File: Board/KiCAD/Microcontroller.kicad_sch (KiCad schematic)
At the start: 26 parts, among them J2 Conn_ARM_SWD_TagConnect_TC2030, J3 Boot, SW2 SW_Push, U10 RT9193-33GB, U2 MIC4680, U9 STM32F103C8T6, Y4 CM8V-T1A-32.768KHZ-12.5PF-20P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, Y5 8MHz

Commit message: Add files via upload
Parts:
- removed C11, C29: 1uF, Capacitor_SMD:C_0201_0603Metric, symbol Device:C_Small
- removed C28: 22nF, Capacitor_SMD:C_0201_0603Metric, symbol Device:C_Small
- removed C45: 15uF, Capacitor_SMD:C_0201_0603Metric, symbol Device:C_Small
- removed C46: ~, Capacitor_SMD:C_0201_0603Metric, symbol Device:C_Small
- removed D1: B260, Diode_SMD:D_SMB, symbol Diode:B260
- removed L1: 10uH, symbol Device:L_Small
- removed R72: 3k, Resistor_SMD:R_0201_0603Metric, symbol Device:R_Small
- removed R73: 1k, Resistor_SMD:R_0201_0603Metric, symbol Device:R_Small
- removed U10: RT9193-33GB, Package_TO_SOT_SMD:SOT-23-5, symbol RT9193-33GB:RT9193-33GB
- removed U2: MIC4680, Package_SO:SOIC-8-1EP_3.9x4.9mm_P1.27mm_EP2.41x3.3mm_ThermalVias, symbol MIC4680:MIC4680
- added C51, C52, C53: 15uF, Capacitor_SMD:C_0201_0603Metric, symbol Device:C_Small
- added L3: 10uH, symbol Device:L_Small
- added U5: LMR50410, Package_TO_SOT_SMD:SOT-23-6, symbol Regulator_Switching:LMR50410
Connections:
- net 3.3V: now also C53.1, L3.2, U5.3 (FB)
- net GND: now also C51.2, C53.2, U5.2 (GND)
- net Vin: now also C51.1, U5.4 (EN), U5.5 (VIN)
- net Thermistor C1: now reaches U9.12 (PA2)
- net Thermistor C2: now reaches U9.13 (PA3)
- net Thermistor C3: now reaches U9.14 (PA4)
- net Thermistor C4: now reaches U9.15 (PA5)
- net SWDIO: now reaches U9.34 (PA13)
- net SWDIO: now also J2.2 (SWDIO), J2.6 (SWO)
- net SWCLK: now reaches U9.37 (PA14)
- net SWCLK: now also J2.4 (SWCLK)
- new net: C52.1, U5.1 (CB)
- new net: C52.2, L3.1, U5.6 (SW)
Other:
- note removed: "Why in the world are you doing an SPS to an LDO? Don't do this, it's expensive, takes realestate, and you absolutely do not need the analog precision this gives. In fact, you're killing the quiet analog supply by connecting it to a microcontroller. So: replace this with a small, simple, SPS that only outputs 3.3V at less than 500 mA."
- moved on the sheet: C30, C31, C32, C33, C34, J2, J3, R58, R59, R60, R75, SW2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

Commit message: Add files via upload
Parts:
- removed J3: Boot, symbol Connector_Generic:Conn_02x03_Top_Bottom
- removed R59: 100k, Resistor_SMD:R_0201_0603Metric, symbol Device:R_Small
- added J4: Conn_01x03, Connector_PinHeader_1.00mm:PinHeader_1x03_P1.00mm_Vertical, symbol Connector_Generic:Conn_01x03
- C34: value 100n -> 100nF
- C51: value 15uF -> 2.2uF
- C52, C53: value 15uF -> 10uF
- L3: value 10uH -> 3.3uH; footprint (none) -> Inductor_SMD:L_10.4x10.4_H4.8
- SW2: footprint (none) -> Button_Switch_SMD:SW_Push_1P1T_NO_CK_KMR2
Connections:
- net 3.3V: now also J4.1 (Pin_1)
- net GND: now also J4.3 (Pin_3)
- net at R58.1: now also J4.2 (Pin_2)
- net Boot1: no longer names the net of U9.20 (PB2)
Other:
- note removed: "You don't need BOOT1"

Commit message: Add files via upload
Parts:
- L3: footprint Inductor_SMD:L_10.4x10.4_H4.8 -> Inductor_SMD:L_1008_2520Metric_Pad1.43x2.20mm_HandSolder
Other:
- note removed: "CONNECT ME"
- note removed: "Can this just be a push button? Like Reset?"
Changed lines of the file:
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@@
 		(comment 3 "Capstone - Team #6")
-	)
-	(text "Can this just be a push button?\nLike Reset?"
-		(exclude_from_sim no)
-		(at 176.53 59.69 0)
-		(effects
-			(font
-				(size 1.27 1.27)
-			)
-		)
 	)
 	(text "LEDS! GIVE ME LEDS! So many status LEDs!"
@@
 		(exclude_from_sim no)
 		(at 171.45 111.76 0)
-		(effects
-			(font
-				(size 1.27 1.27)
-			)
-		)
-	)
-	(text "CONNECT ME"
-		(exclude_from_sim no)
-		(at 151.13 50.8 0)
 		(effects
 			(font
@@
 			)
 		)
-		(property "Footprint" "Inductor_SMD:L_10.4x10.4_H4.8"
+		(property "Footprint" "Inductor_SMD:L_1008_2520Metric_Pad1.43x2.20mm_HandSolder"
 			(at 76.2 45.72 0)
 			(effects

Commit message: Add files via upload
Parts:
- C30, C31, C32, C33, C34, C51: footprint Capacitor_SMD:C_0201_0603Metric -> Capacitor_SMD:C_0603_1608Metric
- C52, C53: footprint Capacitor_SMD:C_0201_0603Metric -> Capacitor_SMD:C_1206_3216Metric; MFR (none) -> SAMSUNG; MPN (none) -> CL31A106KBHNNNE
- J4: footprint Connector_PinHeader_1.00mm:PinHeader_1x03_P1.00mm_Vertical -> Connector_PinHeader_2.54mm:PinHeader_1x03_P2.54mm_Vertical
- R58, R60, R75: footprint Resistor_SMD:R_0201_0603Metric -> Resistor_SMD:R_0603_1608Metric
- U9: MF STMicroelectronics -> (none); MFR (none) -> STMicroelectronics; MP STM32F103C8T6 -> (none); MPN (none) -> STM32F103C8T6
- Y4: MF Micro Crystal AG -> (none); MFR (none) -> Micro Crystal AG; MP CM8V-T1A-32.768KHZ-12.5PF-20PPM-TA-QA -> (none); MPN (none) -> CM8V-T1A-32.768KHZ-12.5PF-20PPM-TA-QA
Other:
- note removed: "LEDS! GIVE ME LEDS! So many status LEDs!"
- note removed: "Power LEDs! Give me all the power LEDs!"
- note removed: "SWD connector, "Tag Connect"."
- moved on the sheet: J2

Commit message: Updated Schematic & PCB Layout
Updated the look of the PCB layout to make the power flow Vin more intuitive.

@KeytarGoblin
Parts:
- C51: footprint Capacitor_SMD:C_0603_1608Metric -> Capacitor_SMD:C_1206_3216Metric
- Y5: footprint Crystal:Crystal_HC49-4H_Vertical -> Crystal:Crystal_SMD_5032-2Pin_5.0x3.2mm
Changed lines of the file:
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@@
 			)
 		)
-		(property "Footprint" "Capacitor_SMD:C_0603_1608Metric"
+		(property "Footprint" "Capacitor_SMD:C_1206_3216Metric"
 			(at 40.64 44.45 0)
 			(effects
@@
 			)
 		)
-		(property "Footprint" "Crystal:Crystal_HC49-4H_Vertical"
+		(property "Footprint" "Crystal:Crystal_SMD_5032-2Pin_5.0x3.2mm"
 			(at 74.93 170.18 0)
 			(effects

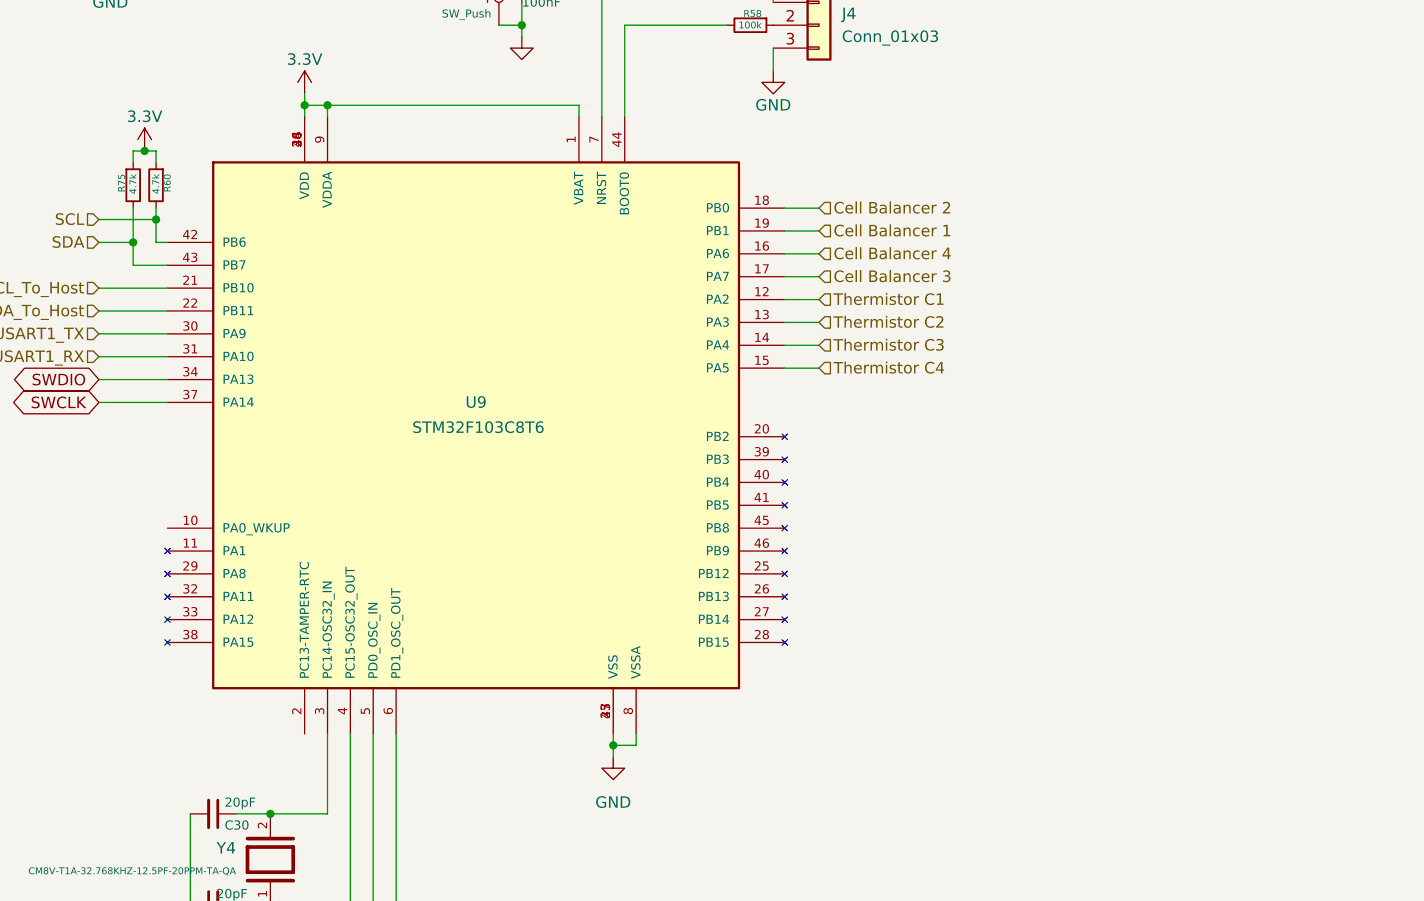
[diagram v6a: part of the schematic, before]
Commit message: Schematic: - Fixed FDI plug - Added thermistor connectors - Added a bunch of NCs using KiCAD NC tool - Added filter cap back into battery current shunt - Added bypass cap to LTC - Removed Cell 4 INA260 because the LTC does current, voltage of that top cell! Board Layout: - Chewed out team for not reading the BQ's datasheet, specifically Section 11 - Relayed out power stream using Section 11 as a refernce - Changed some footprints, mostly reducing size to 0603 - Positioned things optimally given what I thought made sense (dangerous, I know) - Fixed ground planes Other: - Removed PRL and CACHE files from the repo.
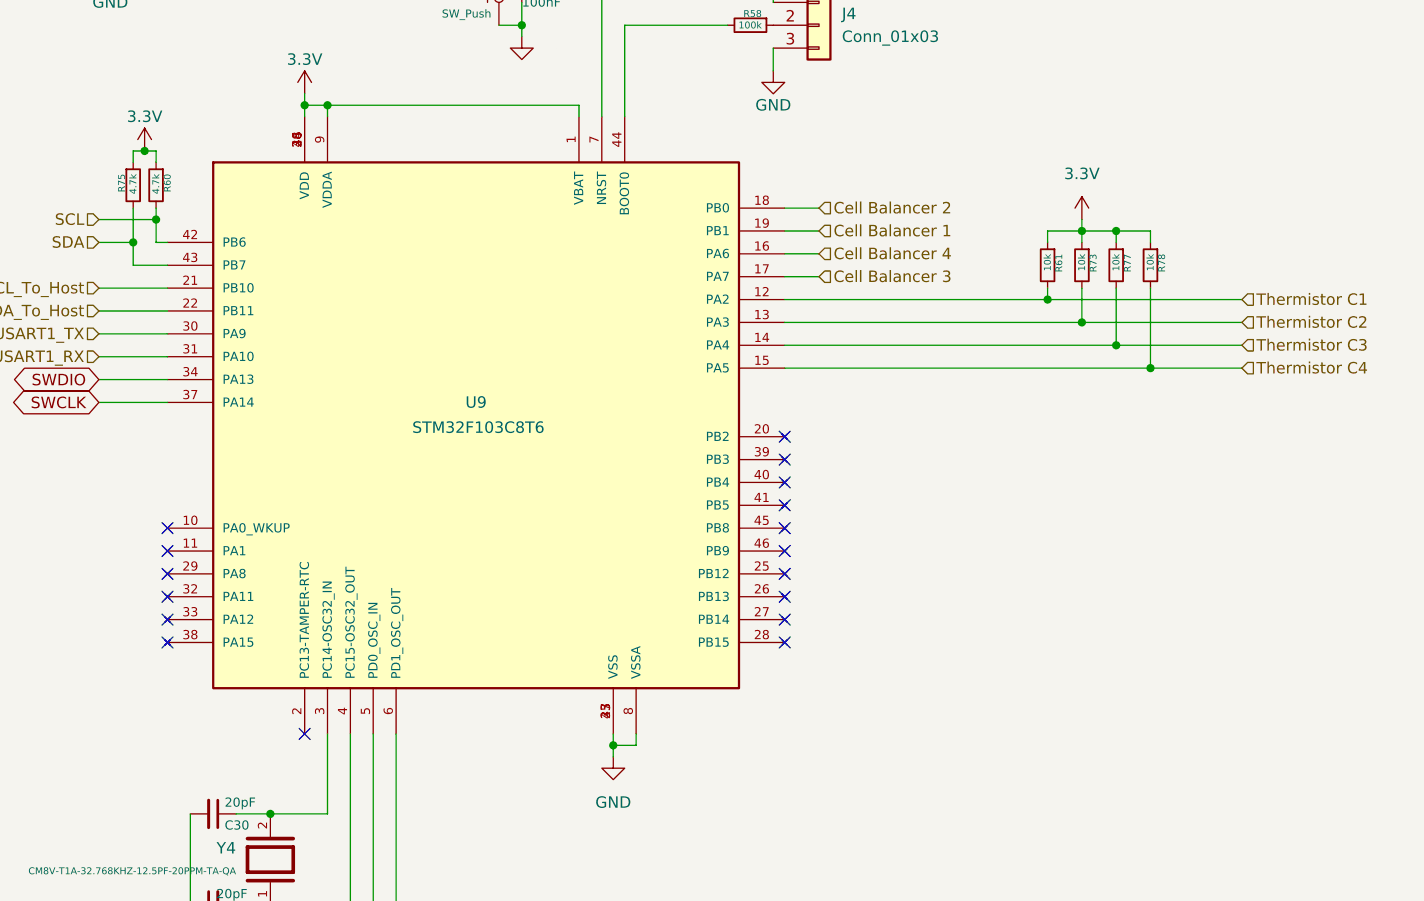
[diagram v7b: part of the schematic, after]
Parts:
- added R61, R73, R77, R78: 10k, Resistor_SMD:R_0603_1608Metric, symbol Device:R_Small
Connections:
- net 3.3V: now also R61.1, R73.1, R77.1, R78.1
- net Thermistor C1: now also R61.2
- net Thermistor C2: now also R73.2
- net Thermistor C3: now also R77.2
- net Thermistor C4: now also R78.2
- no-connect marks 0 -> 17

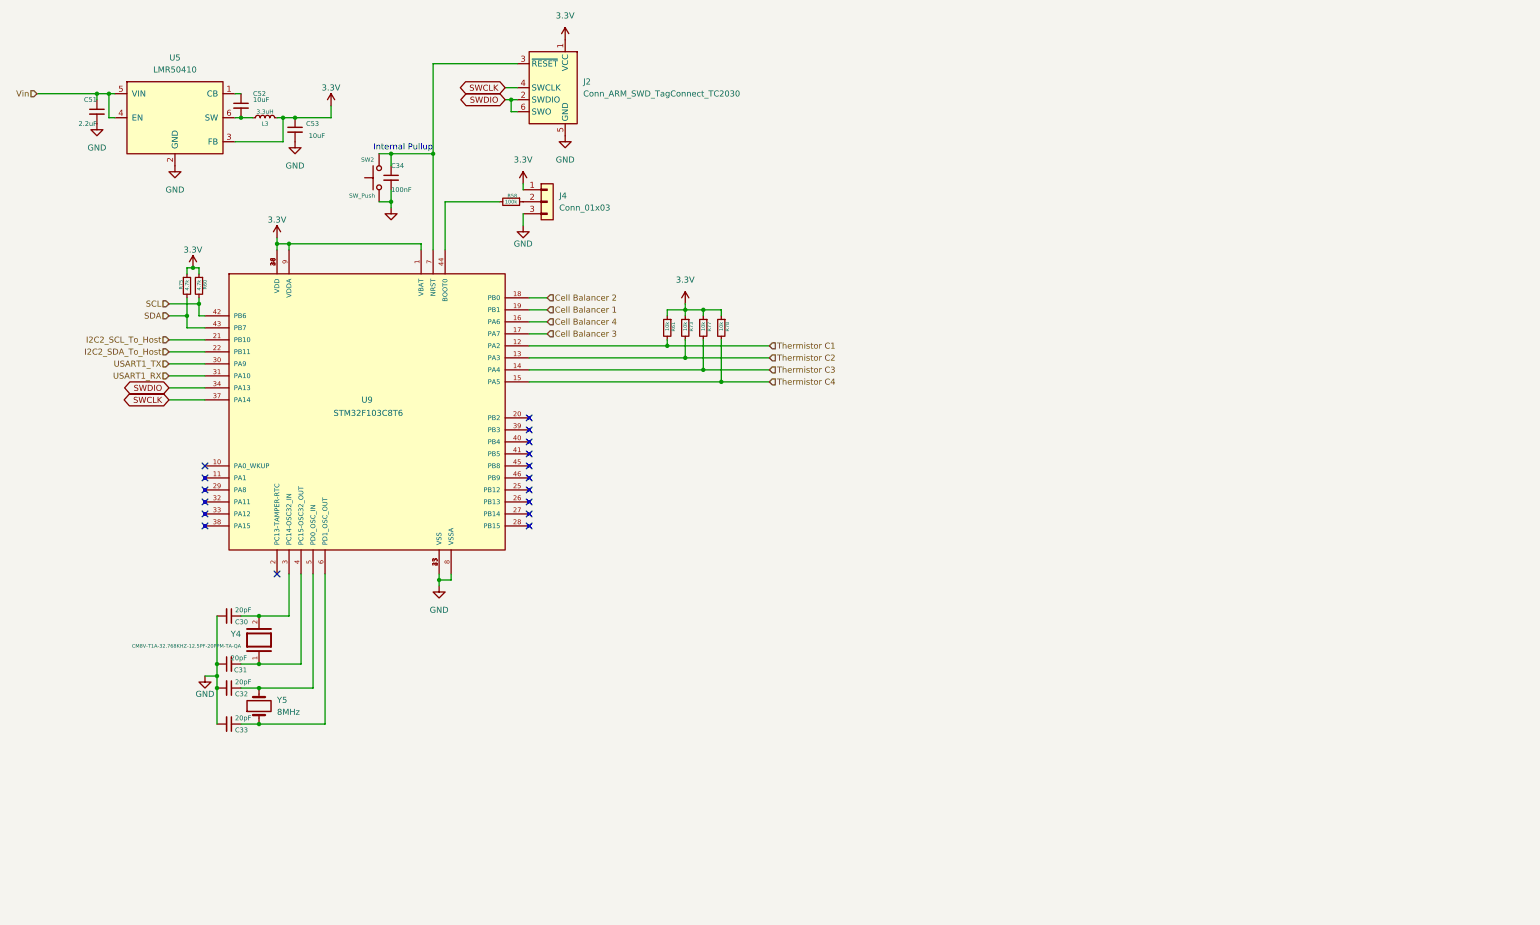
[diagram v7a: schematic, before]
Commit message: Schematic: - Changed to smaller 4 pin crystal - Added STM32 bypass caps Layout: - Added some example zones around vbus - Initial component placement for STM32 - Did an example Kelvin connection for shunt resistors - Added 3.3V power zone on layer 3 (PWR)
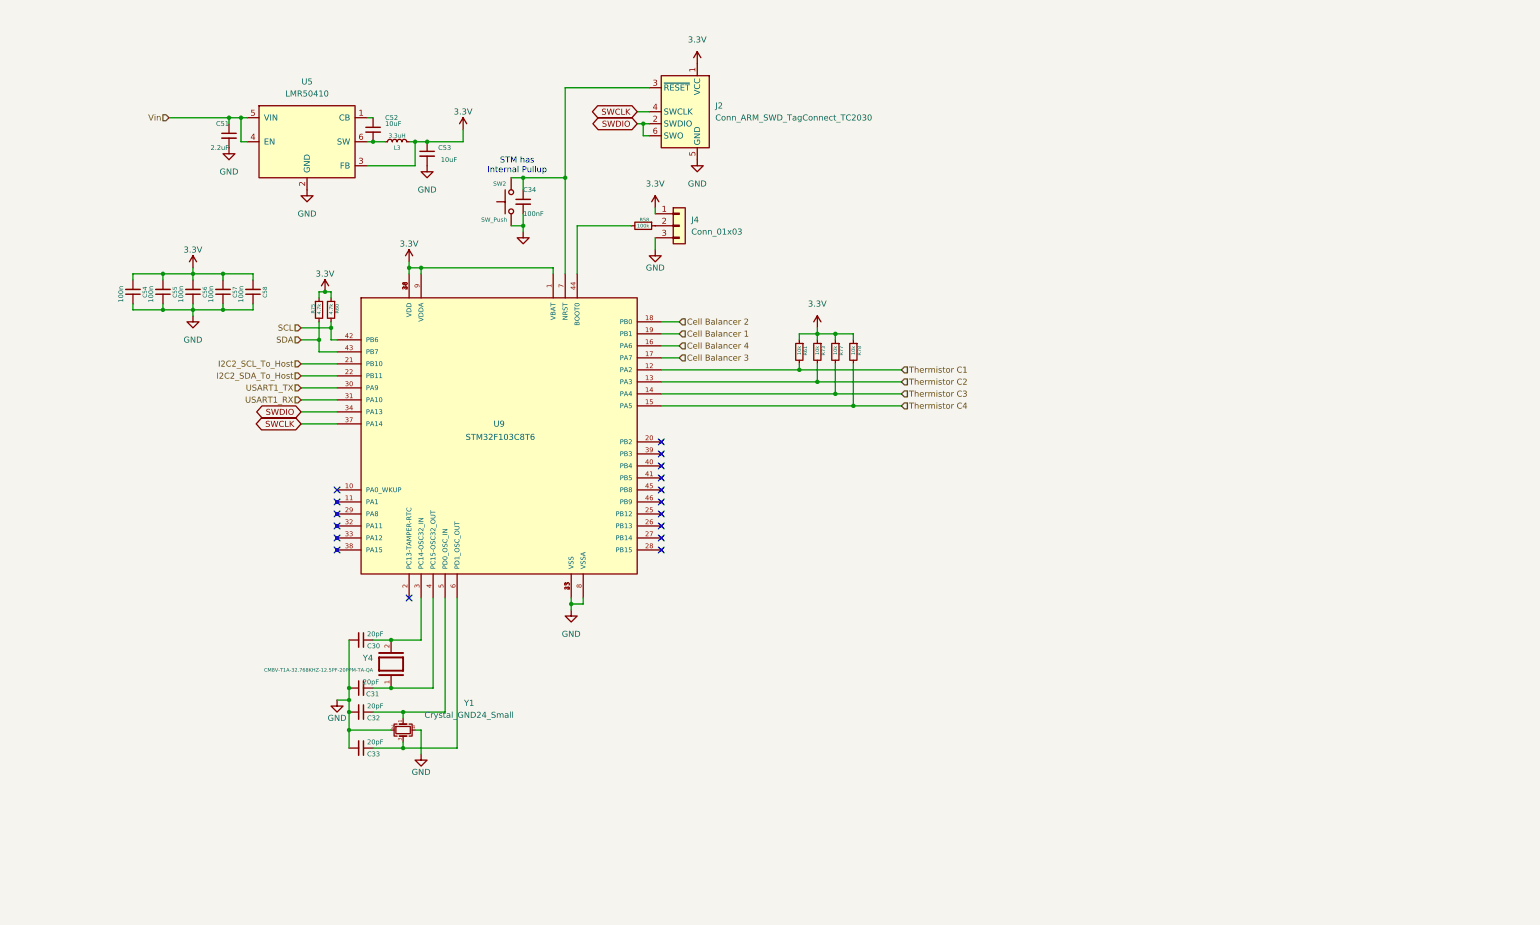
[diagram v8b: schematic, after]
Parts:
- removed Y5: 8MHz, Crystal:Crystal_SMD_5032-2Pin_5.0x3.2mm, symbol Device:Crystal
- added C54, C55, C56, C57, C58: 100n, Capacitor_SMD:C_0603_1608Metric, symbol Device:C_Small
- added Y1: Crystal_GND24_Small, Crystal:Crystal_SMD_TXC_7M-4Pin_3.2x2.5mm, symbol Device:Crystal_GND24_Small
- U9: Availability In Stock -> (none); Check_prices https://www.snapeda.com/parts/STM32F103C8T6/STMicroelectron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 -> (none); Description_1 ARM® Cortex®-M3 STM32F1 Microcontroller IC 32-Bit 72MHz 64K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 -> (none); MANUFACTURER ST Microelectronics -> (none); PARTREV 10 -> (none); Package LQFP-48 STMicroelectronics -> (none); Price None -> (none); STANDARD IPC7351B -> (none); SnapEDA_Link https://www.snapeda.com/parts/STM32F103C8T6/STMicroelectron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 -> (none)
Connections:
- net 3.3V: now also C54.2, C55.2, C56.2, C57.2, C58.2
- net GND: now also C54.1, C55.1, C56.1, C57.1, C58.1, Y1.2, Y1.4
- net at C33.1, U9.6 (PD1_OSC_OUT): now also Y1.3
- net at C32.1, U9.5 (PD0_OSC_IN): now also Y1.1
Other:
- note added: "STM has Internal Pullup"
- note removed: "Internal Pullup"
- moved on the sheet: C30, C31, C32, C33, C34, C51, C52, C53, J2, J4, L3, R58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
